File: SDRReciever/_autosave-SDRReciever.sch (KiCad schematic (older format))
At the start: 80 parts, among them J1 Conn_Coaxial, J10 I_0, J11 I_180, J12 Q_90, J13 Q_270, J14 I_OUT, J15 Q_OUT, J16 5V, J17 4.3V, J18 Conn_01x02_Female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

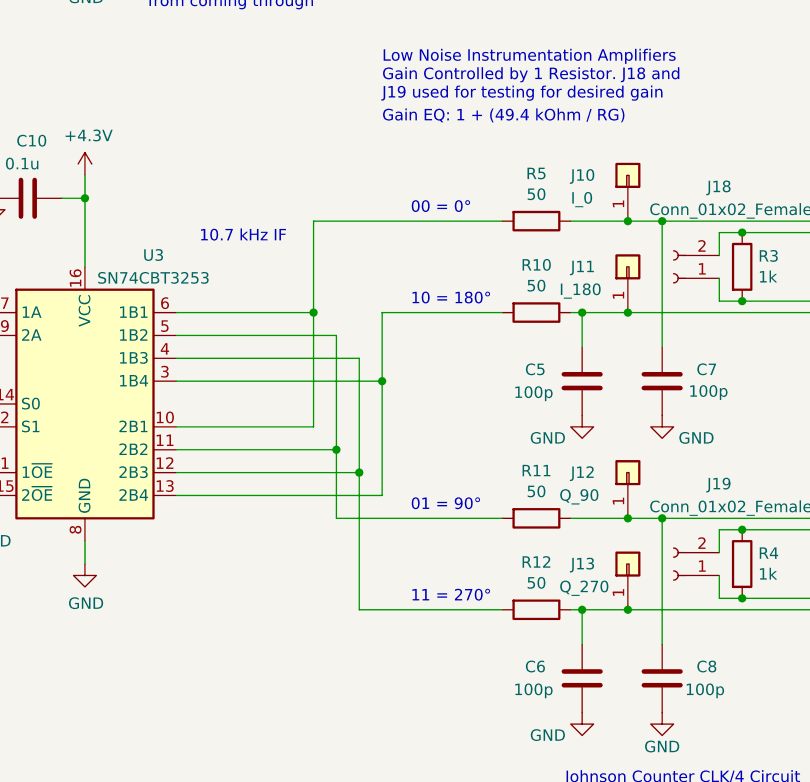
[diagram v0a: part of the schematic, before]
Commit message: Added issue4 testing images
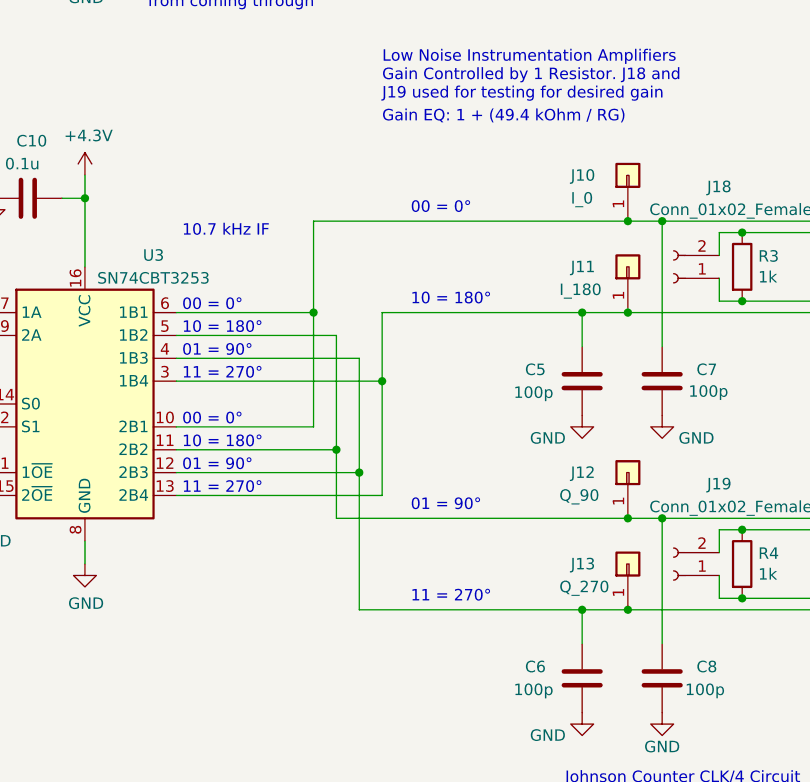
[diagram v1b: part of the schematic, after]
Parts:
- removed R10, R11, R12, R5: 50, Resistor_THT:R_Axial_DIN0207_L6.3mm_D2.5mm_P7.62mm_Horizontal, symbol Device:R
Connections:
- net at C5.1, J11.1 (Pin_1), U4.1 (-IN): now also U3.13 (2B4), U3.3 (1B4)
- net at C6.1, J13.1 (Pin_1), U5.1 (-IN): now also U3.12 (2B3), U3.4 (1B3)
- net at C8.1, J12.1 (Pin_1), U5.4 (+IN): now also U3.11 (2B2), U3.5 (1B2)
- net at C7.1, J10.1 (Pin_1), U4.4 (+IN): now also U3.10 (2B1), U3.6 (1B1)
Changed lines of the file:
@@
 Wire Wire Line
 	1850 6925 1850 6875
-Text Notes 2250 3250 0    50   ~ 0
+Text Notes 2175 3225 0    50   ~ 0
 10.7 kHz IF
-Text Notes 2000 875  0    50   ~ 0
-Bandpass Filter 5-18MHz (3rd Order, Series-First Bessel)\nBy doing Series-First, DC signals cannot pass through the capacitor (C2), \nallowing better control over the DC offset going into the op-amps
-Text Notes 2025 2225 0    50   ~ 0
-Voltage Protection Diodes:\nThese will prevent too large of signals \nfrom coming through
 $Comp
 L power:GND #PWR015
@@
 Low Noise Instrumentation Amplifiers\nGain Controlled by 1 Resistor. J18 and \nJ19 used for testing for desired gain
 $Comp
-L Device:R R5
-U 1 1 5EA72DEC
-P 3725 3150
-F 0 "R5" V 3518 3150 50  0000 C CNN
-F 1 "50" V 3609 3150 50  0000 C CNN
-F 2 "Resistor_THT:R_Axial_DIN0207_L6.3mm_D2.5mm_P7.62mm_Horizontal" V 3655 3150 50  0001 C CNN
-F 3 "~" H 3725 3150 50  0001 C CNN
-	1    3725 3150
-	0    1    1    0
-$EndComp
-$Comp
 L Device:C C5
 U 1 1 5E972924
@@
 $EndComp
 $Comp
-L Device:R R10
-U 1 1 5EAB1A22
-P 3725 3550
-F 0 "R10" V 3518 3550 50  0000 C CNN
-F 1 "50" V 3609 3550 50  0000 C CNN
-F 2 "Resistor_THT:R_Axial_DIN0207_L6.3mm_D2.5mm_P7.62mm_Horizontal" V 3655 3550 50  0001 C CNN
-F 3 "~" H 3725 3550 50  0001 C CNN
-	1    3725 3550
-	0    1    1    0
-$EndComp
-$Comp
 L power:GND #PWR09
 U 1 1 5E9775A8
@@
 	1    0    0    -1
 $EndComp
-$Comp
-L Device:R R11
-U 1 1 5EACF577
-P 3725 4450
-F 0 "R11" V 3518 4450 50  0000 C CNN
-F 1 "50" V 3609 4450 50  0000 C CNN
-F 2 "Resistor_THT:R_Axial_DIN0207_L6.3mm_D2.5mm_P7.62mm_Horizontal" V 3655 4450 50  0001 C CNN
-F 3 "~" H 3725 4450 50  0001 C CNN
-	1    3725 4450
-	0    1    1    0
-$EndComp
-$Comp
-L Device:R R12
-U 1 1 5EACFAEA
-P 3725 4850
-F 0 "R12" V 3518 4850 50  0000 C CNN
-F 1 "50" V 3609 4850 50  0000 C CNN
-F 2 "Resistor_THT:R_Axial_DIN0207_L6.3mm_D2.5mm_P7.62mm_Horizontal" V 3655 4850 50  0001 C CNN
-F 3 "~" H 3725 4850 50  0001 C CNN
-	1    3725 4850
-	0    1    1    0
-$EndComp
-Wire Wire Line
-	3875 3150 4125 3150
 $Comp
 L power:PWR_FLAG #FLG0102
@@
 	5775 4650 6125 4650
 Wire Wire Line
-	3875 3550 3925 3550
-Wire Wire Line
 	4125 3150 4275 3150
 Wire Wire Line
@@
 Connection ~ 4625 4800
 Wire Wire Line
-	3875 4850 3925 4850
-Wire Wire Line
 	4125 4450 4275 4450
-Wire Wire Line
-	3875 4450 4125 4450
 Wire Wire Line
 	4125 4850 4925 4850
@@
 Wire Notes Line
 	3375 1400 3375 1225
-Text Notes 1150 1925 0    50   ~ 0
-Jumper for\npreventing \nground loops
 Wire Notes Line
 	4600 1150 4750 1150
@@
 Text Notes 8500 3125 0    50   ~ 0
 The dual op amp symbol was made\nby me. It is not implying that the V+ of one\nis connected to the V- of the other, but that they\nshare the same power and ground pins
-Wire Wire Line
-	2750 3150 3575 3150
-Wire Wire Line
-	3050 3550 3575 3550
-Wire Wire Line
-	2850 4450 3575 4450
-Wire Wire Line
-	2950 4850 3575 4850
 Text Notes 3175 3125 0    50   ~ 0
 00 = 0°
@@
 Text Notes 3175 4825 0    50   ~ 0
 11 = 270°
+Text Notes 1150 1925 0    50   ~ 0
+Jumper for\npreventing \nground loops
+Text Notes 2000 875  0    50   ~ 0
+Bandpass Filter 5-18MHz (3rd Order, Series-First Bessel)\nBy doing Series-First, DC signals cannot pass through the capacitor (C2), \nallowing better control over the DC offset going into the op-amps
+Text Notes 2025 2225 0    50   ~ 0
+Voltage Protection Diodes:\nThese will prevent too large of signals \nfrom coming through
+Text Notes 2175 3550 0    50   ~ 0
+00 = 0°
+Text Notes 2175 4050 0    50   ~ 0
+00 = 0°
+Text Notes 2175 3650 0    50   ~ 0
+10 = 180°
+Text Notes 2175 4150 0    50   ~ 0
+10 = 180°
+Text Notes 2175 3750 0    50   ~ 0
+01 = 90°
+Text Notes 2175 4250 0    50   ~ 0
+01 = 90°
+Text Notes 2175 4350 0    50   ~ 0
+11 = 270°
+Text Notes 2175 3850 0    50   ~ 0
+11 = 270°
+Wire Wire Line
+	2750 3150 4125 3150
+Wire Wire Line
+	3050 3550 3925 3550
+Wire Wire Line
+	2850 4450 4125 4450
+Wire Wire Line
+	2950 4850 3925 4850
 $EndSCHEMATC
